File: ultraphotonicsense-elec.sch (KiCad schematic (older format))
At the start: 6 parts, among them J1 Conn_SWD_UART, Q1 BSS138, U1 74HC164

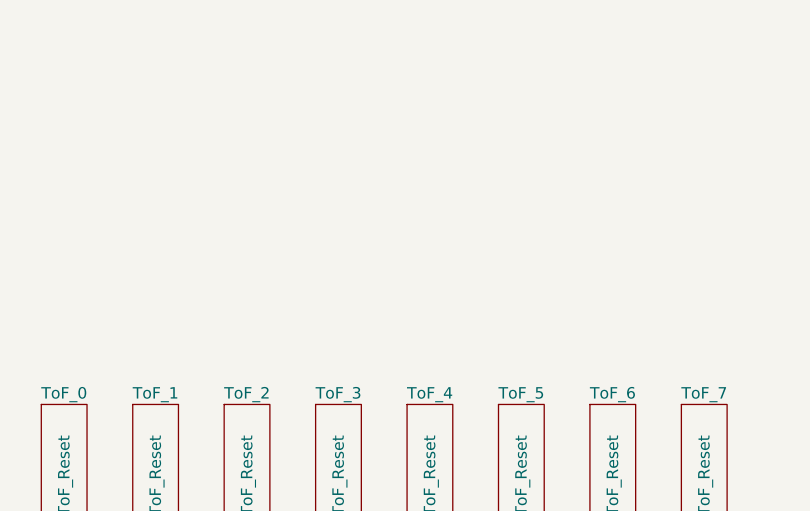
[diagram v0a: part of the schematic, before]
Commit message: Added mounting holes
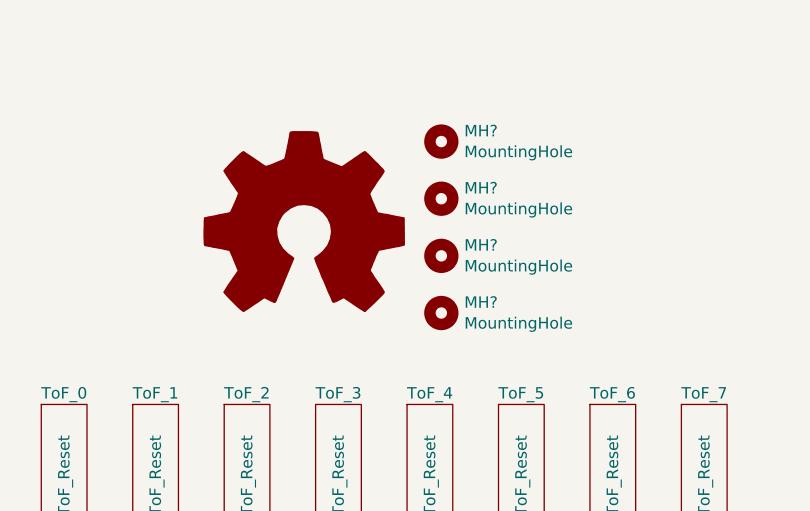
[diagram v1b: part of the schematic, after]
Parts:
- added MH? (x4): MountingHole, symbol Mechanical:MountingHole
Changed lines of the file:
@@
 EESchema Schematic File Version 4
-LIBS:photonicsense-elec-cache
+LIBS:ultraphotonicsense-elec-cache
 EELAYER 26 0
 EELAYER END
@@
 Wire Wire Line
 	1650 3050 1650 2950
+$Comp
+L Graphic:Logo_Open_Hardware_Large #LOGO?
+U 1 1 5BBE6179
+P 8650 3050
+F 0 "#LOGO?" H 8650 3550 50  0001 C CNN
+F 1 "Logo_Open_Hardware_Large" H 8650 2650 50  0001 C CNN
+F 2 "" H 8650 3050 50  0001 C CNN
+F 3 "~" H 8650 3050 50  0001 C CNN
+	1    8650 3050
+	1    0    0    -1
+$EndComp
+$Comp
+L Mechanical:MountingHole MH?
+U 1 1 5BBE6263
+P 9250 2650
+F 0 "MH?" H 9350 2696 50  0000 L CNN
+F 1 "MountingHole" H 9350 2605 50  0000 L CNN
+F 2 "" H 9250 2650 50  0001 C CNN
+F 3 "~" H 9250 2650 50  0001 C CNN
+	1    9250 2650
+	1    0    0    -1
+$EndComp
+$Comp
+L Mechanical:MountingHole MH?
+U 1 1 5BBE62B0
+P 9250 2900
+F 0 "MH?" H 9350 2946 50  0000 L CNN
+F 1 "MountingHole" H 9350 2855 50  0000 L CNN
+F 2 "" H 9250 2900 50  0001 C CNN
+F 3 "~" H 9250 2900 50  0001 C CNN
+	1    9250 2900
+	1    0    0    -1
+$EndComp
+$Comp
+L Mechanical:MountingHole MH?
+U 1 1 5BBE62F0
+P 9250 3150
+F 0 "MH?" H 9350 3196 50  0000 L CNN
+F 1 "MountingHole" H 9350 3105 50  0000 L CNN
+F 2 "" H 9250 3150 50  0001 C CNN
+F 3 "~" H 9250 3150 50  0001 C CNN
+	1    9250 3150
+	1    0    0    -1
+$EndComp
+$Comp
+L Mechanical:MountingHole MH?
+U 1 1 5BBE6333
+P 9250 3400
+F 0 "MH?" H 9350 3446 50  0000 L CNN
+F 1 "MountingHole" H 9350 3355 50  0000 L CNN
+F 2 "" H 9250 3400 50  0001 C CNN
+F 3 "~" H 9250 3400 50  0001 C CNN
+	1    9250 3400
+	1    0    0    -1
+$EndComp
 $EndSCHEMATC

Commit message: Fixed shift register voltage translation
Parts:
- removed Q1: BSS138, Package_TO_SOT_SMD:SOT-23, symbol Transistor_FET:BSS138
- removed R1, R2: R, symbol Device:R
- gave numbers to parts that had none: 4
- renumbered JP2 to JP1
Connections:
- wire segments 70 -> 66

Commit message: Fixed TTa pins issue
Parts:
- removed JP1: Jumper_NC_Dual, symbol Device:Jumper_NC_Dual
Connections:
- net labels removed: US_POWER
- wire segments 66 -> 63

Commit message: Added IC for level translation with ultrasonic sensors
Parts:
- added C1, C2: C, symbol Device:C
- added R1: R, symbol Device:R
- added U1: TXB0108PW, Package_SO:TSSOP-20_4.4x6.5mm_P0.65mm, symbol PhoenixRobotik:TXB0108PW
- J1: footprint (none) -> Connector_JST:JST_XH_S08B-XH-A_1x08_P2.50mm_Horizontal
- MH1, MH2, MH3, MH4: footprint (none) -> MountingHole:MountingHole_2.7mm_M2.5
- U2: renamed from U1; footprint (none) -> Package_SO:SOIC-14_3.9x8.7mm_P1.27mm
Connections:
- wire segments 63 -> 94
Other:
- moved on the sheet: MH1, MH2, MH3, MH4, U2

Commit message: Added ultrasonic sensors power selection
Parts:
- added JP2: Jumper_NC_Dual, symbol Device:Jumper_NC_Dual
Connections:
- net labels added: US_PWR
- wire segments 94 -> 100
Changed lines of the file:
@@
 	5550 2900 5550 3050
-$Comp
-L power:+5V #PWR09
-U 1 1 5BC0FF87
-P 5750 2450
-F 0 "#PWR09" H 5750 2300 50  0001 C CNN
-F 1 "+5V" H 5765 2623 50  0000 C CNN
-F 2 "" H 5750 2450 50  0001 C CNN
-F 3 "" H 5750 2450 50  0001 C CNN
-	1    5750 2450
-	1    0    0    -1
-$EndComp
 $Comp
 L Device:C C1
@@
 	-1   0    0    1
 $EndComp
+Wire Wire Line
+	5350 2900 5550 2900
+Wire Wire Line
+	5550 2900 5550 2450
+Connection ~ 5550 2900
+$Comp
+L power:GND #PWR075
+U 1 1 5BC5DA99
+P 5950 2450
+F 0 "#PWR075" H 5950 2200 50  0001 C CNN
+F 1 "GND" H 5955 2277 50  0000 C CNN
+F 2 "" H 5950 2450 50  0001 C CNN
+F 3 "" H 5950 2450 50  0001 C CNN
+	1    5950 2450
+	-1   0    0    1
+$EndComp
+Wire Wire Line
+	5750 3050 5750 2900
+Wire Wire Line
+	5750 2900 5950 2900
+Connection ~ 5750 2900
+Wire Wire Line
+	5750 2900 5750 2450
+$Comp
+L Device:Jumper_NC_Dual JP2
+U 1 1 5BC62830
+P 1650 2650
+F 0 "JP2" V 1604 2751 50  0000 L CNN
+F 1 "Jumper_NC_Dual" V 1695 2751 50  0000 L CNN
+F 2 "" H 1650 2650 50  0001 C CNN
+F 3 "~" H 1650 2650 50  0001 C CNN
+	1    1650 2650
+	0    1    1    0
+$EndComp
+Text GLabel 1400 2650 0    50   Output ~ 0
+US_PWR
+Wire Wire Line
+	1400 2650 1500 2650
+$Comp
+L power:+5V #PWR09
+U 1 1 5BC6506A
+P 1650 2250
+F 0 "#PWR09" H 1650 2100 50  0001 C CNN
+F 1 "+5V" H 1665 2423 50  0000 C CNN
+F 2 "" H 1650 2250 50  0001 C CNN
+F 3 "" H 1650 2250 50  0001 C CNN
+	1    1650 2250
+	1    0    0    -1
+$EndComp
+Wire Wire Line
+	1650 2250 1650 2400
+$Comp
+L power:+3V3 #PWR048
+U 1 1 5BC678E1
+P 1650 3050
+F 0 "#PWR048" H 1650 2900 50  0001 C CNN
+F 1 "+3V3" H 1665 3223 50  0000 C CNN
+F 2 "" H 1650 3050 50  0001 C CNN
+F 3 "" H 1650 3050 50  0001 C CNN
+	1    1650 3050
+	-1   0    0    1
+$EndComp
+Wire Wire Line
+	1650 2900 1650 3050
 $Comp
 L power:+3.3V #PWR074
@@
 	1    0    0    -1
 $EndComp
-Wire Wire Line
-	5350 2900 5550 2900
-Wire Wire Line
-	5550 2900 5550 2450
-Connection ~ 5550 2900
-$Comp
-L power:GND #PWR075
-U 1 1 5BC5DA99
-P 5950 2450
-F 0 "#PWR075" H 5950 2200 50  0001 C CNN
-F 1 "GND" H 5955 2277 50  0000 C CNN
-F 2 "" H 5950 2450 50  0001 C CNN
-F 3 "" H 5950 2450 50  0001 C CNN
-	1    5950 2450
-	-1   0    0    1
-$EndComp
-Wire Wire Line
-	5750 3050 5750 2900
-Wire Wire Line
-	5750 2900 5950 2900
-Connection ~ 5750 2900
-Wire Wire Line
-	5750 2900 5750 2450
+Text GLabel 5750 2450 1    50   Input ~ 0
+US_PWR
+$Comp
+L power:PWR_FLAG #FLG04
+U 1 1 5BC6A929
+P 1400 2800
+F 0 "#FLG04" H 1400 2875 50  0001 C CNN
+F 1 "PWR_FLAG" V 1400 2928 50  0000 L CNN
+F 2 "" H 1400 2800 50  0001 C CNN
+F 3 "~" H 1400 2800 50  0001 C CNN
+	1    1400 2800
+	0    -1   -1   0
+$EndComp
+Wire Wire Line
+	1500 2650 1500 2800
+Wire Wire Line
+	1500 2800 1400 2800
+Connection ~ 1500 2650
+Wire Wire Line
+	1500 2650 1550 2650
 $EndSCHEMATC

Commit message: Footprint association
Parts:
- C1, C2: footprint (none) -> Capacitor_SMD:C_0805_2012Metric_Pad1.15x1.40mm_HandSolder
- JP2: footprint (none) -> Connector_PinHeader_2.54mm:PinHeader_1x03_P2.54mm_Vertical
- R1: footprint (none) -> Resistor_SMD:R_0805_2012Metric_Pad1.15x1.40mm_HandSolder
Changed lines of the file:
@@
 F 0 "C1" H 5236 2704 50  0000 R CNN
 F 1 "C" H 5236 2795 50  0000 R CNN
-F 2 "" H 5388 2600 50  0001 C CNN
+F 2 "Capacitor_SMD:C_0805_2012Metric_Pad1.15x1.40mm_HandSolder" H 5388 2600 50  0001 C CNN
 F 3 "~" H 5350 2750 50  0001 C CNN
 	1    5350 2750
@@
 F 0 "C2" H 6065 2796 50  0000 L CNN
 F 1 "C" H 6065 2705 50  0000 L CNN
-F 2 "" H 5988 2600 50  0001 C CNN
+F 2 "Capacitor_SMD:C_0805_2012Metric_Pad1.15x1.40mm_HandSolder" H 5988 2600 50  0001 C CNN
 F 3 "~" H 5950 2750 50  0001 C CNN
 	1    5950 2750
@@
 F 0 "R1" H 5120 3146 50  0000 L CNN
 F 1 "R" H 5120 3055 50  0000 L CNN
-F 2 "" V 4980 3100 50  0001 C CNN
+F 2 "Resistor_SMD:R_0805_2012Metric_Pad1.15x1.40mm_HandSolder" V 4980 3100 50  0001 C CNN
 F 3 "~" H 5050 3100 50  0001 C CNN
 	1    5050 3100
@@
 F 0 "JP2" V 1604 2751 50  0000 L CNN
 F 1 "Jumper_NC_Dual" V 1695 2751 50  0000 L CNN
-F 2 "" H 1650 2650 50  0001 C CNN
+F 2 "Connector_PinHeader_2.54mm:PinHeader_1x03_P2.54mm_Vertical" H 1650 2650 50  0001 C CNN
 F 3 "~" H 1650 2650 50  0001 C CNN
 	1    1650 2650

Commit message: Schematic corrections
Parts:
- J1: footprint Connector_JST:JST_XH_S08B-XH-A_1x08_P2.50mm_Horizontal -> Connector_JST:JST_PH_B8B-PH-K_1x08_P2.00mm_Vertical
- renumbered JP2 to JP1
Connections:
- wire segments 100 -> 98
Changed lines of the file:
@@
 $EndSheet
 $Comp
-L power:+3.3V #PWR01
+L power:+3.3V #PWR03
 U 1 1 5BBBF8DE
 P 2300 4050
-F 0 "#PWR01" H 2300 3900 50  0001 C CNN
+F 0 "#PWR03" H 2300 3900 50  0001 C CNN
 F 1 "+3.3V" V 2315 4178 50  0000 L CNN
 F 2 "" H 2300 4050 50  0001 C CNN
@@
 $EndComp
 $Comp
-L power:+2V8 #PWR02
+L power:+2V8 #PWR04
 U 1 1 5BBBF9EE
 P 2300 4150
-F 0 "#PWR02" H 2300 4000 50  0001 C CNN
+F 0 "#PWR04" H 2300 4000 50  0001 C CNN
 F 1 "+2V8" V 2315 4278 50  0000 L CNN
 F 2 "" H 2300 4150 50  0001 C CNN
@@
 F 0 "J1" V 3117 2646 50  0000 C CNN
 F 1 "Conn_SWD_UART" V 3026 2646 50  0000 C CNN
-F 2 "Connector_JST:JST_XH_S08B-XH-A_1x08_P2.50mm_Horizontal" H 2900 2700 50  0001 C CNN
+F 2 "Connector_JST:JST_PH_B8B-PH-K_1x08_P2.00mm_Vertical" H 2900 2700 50  0001 C CNN
 F 3 "~" H 2900 2700 50  0001 C CNN
 	1    2900 2700
@@
 	2900 3700 3550 3700
 $Comp
-L power:GND #PWR05
+L power:GND #PWR07
 U 1 1 5BBC1836
 P 2800 3000
-F 0 "#PWR05" H 2800 2750 50  0001 C CNN
+F 0 "#PWR07" H 2800 2750 50  0001 C CNN
 F 1 "GND" H 2805 2827 50  0000 C CNN
 F 2 "" H 2800 3000 50  0001 C CNN
@@
 	2700 3800 3550 3800
 $Comp
-L power:+3V3 #PWR04
+L power:+3V3 #PWR06
 U 1 1 5BBC19E2
 P 2600 3000
-F 0 "#PWR04" H 2600 2850 50  0001 C CNN
+F 0 "#PWR06" H 2600 2850 50  0001 C CNN
 F 1 "+3V3" H 2615 3173 50  0000 C CNN
 F 2 "" H 2600 3000 50  0001 C CNN
@@
 	1650 4600 1550 4600
 $Comp
-L power:+5V #PWR03
+L power:+5V #PWR05
 U 1 1 5BBF5CE3
 P 2300 4250
-F 0 "#PWR03" H 2300 4100 50  0001 C CNN
+F 0 "#PWR05" H 2300 4100 50  0001 C CNN
 F 1 "+5V" V 2315 4378 50  0000 L CNN
 F 2 "" H 2300 4250 50  0001 C CNN
@@
 	2950 4700 3550 4700
 $Comp
-L power:+2V8 #PWR011
+L power:+2V8 #PWR014
 U 1 1 5BC03D97
 P 7050 4500
-F 0 "#PWR011" H 7050 4350 50  0001 C CNN
+F 0 "#PWR014" H 7050 4350 50  0001 C CNN
 F 1 "+2V8" H 7065 4673 50  0000 C CNN
 F 2 "" H 7050 4500 50  0001 C CNN
@@
 $EndComp
 $Comp
-L power:GND #PWR012
+L power:GND #PWR015
 U 1 1 5BC03E07
 P 7050 6050
-F 0 "#PWR012" H 7050 5800 50  0001 C CNN
+F 0 "#PWR015" H 7050 5800 50  0001 C CNN
 F 1 "GND" H 7055 5877 50  0000 C CNN
 F 2 "" H 7050 6050 50  0001 C CNN
@@
 $EndComp
 $Sheet
-S 6200 2450 300  550
+S 7700 2450 300  550
 U 5BC0526F
 F0 "US_0" 50
 F1 "US.sch" 50
-F2 "Trigger" I B 6300 3000 50
-F3 "Echo" O B 6400 3000 50
-$EndSheet
-$Sheet
-S 6700 2450 300  550
+F2 "Trigger" I B 7900 3000 50
+F3 "Echo" O B 7800 3000 50
+$EndSheet
+$Sheet
+S 7200 2450 300  550
 U 5BC05277
 F0 "US_1" 50
 F1 "US.sch" 50
-F2 "Trigger" I B 6800 3000 50
-F3 "Echo" O B 6900 3000 50
-$EndSheet
-$Sheet
-S 7200 2450 300  550
+F2 "Trigger" I B 7400 3000 50
+F3 "Echo" O B 7300 3000 50
+$EndSheet
+$Sheet
+S 6700 2450 300  550
 U 5BC05284
 F0 "US_2" 50
 F1 "US.sch" 50
-F2 "Trigger" I B 7300 3000 50
-F3 "Echo" O B 7400 3000 50
-$EndSheet
-$Sheet
-S 7700 2450 300  550
+F2 "Trigger" I B 6900 3000 50
+F3 "Echo" O B 6800 3000 50
+$EndSheet
+$Sheet
+S 6200 2450 300  550
 U 5BC05291
 F0 "US_3" 50
 F1 "US.sch" 50
-F2 "Trigger" I B 7800 3000 50
-F3 "Echo" O B 7900 3000 50
+F2 "Trigger" I B 6400 3000 50
+F3 "Echo" O B 6300 3000 50
 $EndSheet
 $Comp
@@
 $EndSheet
 Wire Wire Line
-	6050 5650 6150 5650
-Wire Wire Line
-	6150 5650 6150 5550
-Wire Wire Line
-	6150 5550 6550 5550
-Connection ~ 3450 4300
-Wire Wire Line
 	7050 4500 7050 4650
 $Comp
-L power:+2V8 #PWR010
+L power:+2V8 #PWR013
 U 1 1 5BBFB7FF
 P 6450 5050
-F 0 "#PWR010" H 6450 4900 50  0001 C CNN
+F 0 "#PWR013" H 6450 4900 50  0001 C CNN
 F 1 "+2V8" V 6465 5178 50  0000 L CNN
 F 2 "" H 6450 5050 50  0001 C CNN
@@
 F6 "SWDIO" B L 3550 3700 50
 F7 "SWCLK" I L 3550 3800 50
-F8 "I2C_SCL" B L 3550 4600 50
-F9 "I2C_SDA" B L 3550 4700 50
+F8 "I2C_SCL" B L 3550 4700 50
+F9 "I2C_SDA" B L 3550 4600 50
 F10 "NRST" I L 3550 3600 50
 F11 "TOF_RESET_DATA" O R 4850 4500 50
 F12 "TOF_RESET_SHIFT" O R 4850 4600 50
-F13 "US_TRIG_0" O R 4850 3450 50
-F14 "US_TRIG_1" O R 4850 3650 50
-F15 "US_TRIG_2" O R 4850 3850 50
-F16 "US_TRIG_3" O R 4850 4050 50
-F17 "US_ECHO_0" I R 4850 3550 50
-F18 "US_ECHO_1" I R 4850 3750 50
-F19 "US_ECHO_2" I R 4850 3950 50
-F20 "US_ECHO_3" I R 4850 4150 50
+F13 "US_TRIG_0" O R 4850 4150 50
+F14 "US_TRIG_1" O R 4850 3950 50
+F15 "US_TRIG_2" O R 4850 3750 50
+F16 "US_TRIG_3" O R 4850 3550 50
+F17 "US_ECHO_0" I R 4850 4050 50
+F18 "US_ECHO_1" I R 4850 3850 50
+F19 "US_ECHO_2" I R 4850 3650 50
+F20 "US_ECHO_3" I R 4850 3450 50
 F21 "US_OE" O R 4850 3350 50
 $EndSheet
@@
 	1    0    0    -1
 $EndComp
-Wire Wire Line
-	6150 5300 6150 5250
-Wire Wire Line
-	6150 5250 6550 5250
-Wire Wire Line
-	6050 5300 6150 5300
 $Sheet
 S 5250 5200 800  200
@@
 Wire Wire Line
 	4850 4150 5250 4150
-Wire Wire Line
-	6300 3000 6300 3450
-Wire Wire Line
-	6300 3450 6050 3450
-Wire Wire Line
-	6400 3000 6400 3550
-Wire Wire Line
-	6400 3550 6050 3550
-Wire Wire Line
-	6800 3000 6800 3650
-Wire Wire Line
-	6800 3650 6050 3650
-Wire Wire Line
-	6900 3000 6900 3750
-Wire Wire Line
-	6900 3750 6050 3750
-Wire Wire Line
-	7300 3000 7300 3850
-Wire Wire Line
-	7300 3850 6050 3850
-Wire Wire Line
-	7400 3000 7400 3950
-Wire Wire Line
-	7400 3950 6050 3950
-Wire Wire Line
-	7800 3000 7800 4050
-Wire Wire Line
-	7800 4050 6050 4050
-Wire Wire Line
-	7900 3000 7900 4150
-Wire Wire Line
-	7900 4150 6050 4150
-$Comp
-L power:GND #PWR08
+$Comp
+L power:GND #PWR011
 U 1 1 5BC36ECA
 P 5650 4550
-F 0 "#PWR08" H 5650 4300 50  0001 C CNN
+F 0 "#PWR011" H 5650 4300 50  0001 C CNN
 F 1 "GND" H 5655 4377 50  0000 C CNN
 F 2 "" H 5650 4550 50  0001 C CNN
@@
 	4850 3350 5050 3350
 $Comp
-L power:GND #PWR06
+L power:GND #PWR08
 U 1 1 5BC3D4FD
 P 5050 2850
-F 0 "#PWR06" H 5050 2600 50  0001 C CNN
+F 0 "#PWR08" H 5050 2600 50  0001 C CNN
 F 1 "GND" H 5055 2677 50  0000 C CNN
 F 2 "" H 5050 2850 50  0001 C CNN
@@
 	5050 2850 5050 2950
 Wire Wire Line
-	3450 5650 5250 5650
-Wire Wire Line
-	3450 4300 3450 5650
-Wire Wire Line
 	5250 5300 5000 5300
 Wire Wire Line
@@
 Wire Wire Line
 	5100 4950 5250 4950
-Wire Wire Line
-	5650 4450 5650 4550
-$Comp
-L power:GND #PWR07
+$Comp
+L power:GND #PWR09
 U 1 1 5BC52828
 P 5350 2450
-F 0 "#PWR07" H 5350 2200 50  0001 C CNN
+F 0 "#PWR09" H 5350 2200 50  0001 C CNN
 F 1 "GND" H 5355 2277 50  0000 C CNN
 F 2 "" H 5350 2450 50  0001 C CNN
@@
 Connection ~ 5550 2900
 $Comp
-L power:GND #PWR075
+L power:GND #PWR012
 U 1 1 5BC5DA99
 P 5950 2450
-F 0 "#PWR075" H 5950 2200 50  0001 C CNN
+F 0 "#PWR012" H 5950 2200 50  0001 C CNN
 F 1 "GND" H 5955 2277 50  0000 C CNN
 F 2 "" H 5950 2450 50  0001 C CNN
@@
 	5750 2900 5750 2450
 $Comp
-L Device:Jumper_NC_Dual JP2
+L Device:Jumper_NC_Dual JP1
 U 1 1 5BC62830
 P 1650 2650
-F 0 "JP2" V 1604 2751 50  0000 L CNN
+F 0 "JP1" V 1604 2751 50  0000 L CNN
 F 1 "Jumper_NC_Dual" V 1695 2751 50  0000 L CNN
 F 2 "Connector_PinHeader_2.54mm:PinHeader_1x03_P2.54mm_Vertical" H 1650 2650 50  0001 C CNN
@@
 	1400 2650 1500 2650
 $Comp
-L power:+5V #PWR09
+L power:+5V #PWR01
 U 1 1 5BC6506A
 P 1650 2250
-F 0 "#PWR09" H 1650 2100 50  0001 C CNN
+F 0 "#PWR01" H 1650 2100 50  0001 C CNN
 F 1 "+5V" H 1665 2423 50  0000 C CNN
 F 2 "" H 1650 2250 50  0001 C CNN
@@
 	1650 2250 1650 2400
 $Comp
-L power:+3V3 #PWR048
+L power:+3V3 #PWR02
 U 1 1 5BC678E1
 P 1650 3050
-F 0 "#PWR048" H 1650 2900 50  0001 C CNN
+F 0 "#PWR02" H 1650 2900 50  0001 C CNN
 F 1 "+3V3" H 1665 3223 50  0000 C CNN
 F 2 "" H 1650 3050 50  0001 C CNN
@@
 	1650 2900 1650 3050
 $Comp
-L power:+3.3V #PWR074
+L power:+3.3V #PWR010
 U 1 1 5BC56E1A
 P 5550 2450
-F 0 "#PWR074" H 5550 2300 50  0001 C CNN
+F 0 "#PWR010" H 5550 2300 50  0001 C CNN
 F 1 "+3.3V" H 5565 2623 50  0000 C CNN
 F 2 "" H 5550 2450 50  0001 C CNN
@@
 US_PWR
 $Comp
-L power:PWR_FLAG #FLG04
+L power:PWR_FLAG #FLG01
 U 1 1 5BC6A929
 P 1400 2800
-F 0 "#FLG04" H 1400 2875 50  0001 C CNN
+F 0 "#FLG01" H 1400 2875 50  0001 C CNN
 F 1 "PWR_FLAG" V 1400 2928 50  0000 L CNN
 F 2 "" H 1400 2800 50  0001 C CNN
@@
 Wire Wire Line
 	1500 2650 1550 2650
+Wire Wire Line
+	5650 4450 5650 4550
+Wire Wire Line
+	6400 3550 6050 3550
+Wire Wire Line
+	6400 3000 6400 3550
+Wire Wire Line
+	6300 3450 6050 3450
+Wire Wire Line
+	6300 3000 6300 3450
+Wire Wire Line
+	7900 4150 6050 4150
+Wire Wire Line
+	7900 3000 7900 4150
+Wire Wire Line
+	7800 4050 6050 4050
+Wire Wire Line
+	7800 3000 7800 4050
+Wire Wire Line
+	7400 3950 6050 3950
+Wire Wire Line
+	7400 3000 7400 3950
+Wire Wire Line
+	7300 3850 6050 3850
+Wire Wire Line
+	7300 3000 7300 3850
+Wire Wire Line
+	6900 3750 6050 3750
+Wire Wire Line
+	6900 3000 6900 3750
+Wire Wire Line
+	6800 3650 6050 3650
+Wire Wire Line
+	6800 3000 6800 3650
+Wire Wire Line
+	3450 4300 3450 5650
+Wire Wire Line
+	3450 5650 5250 5650
+Connection ~ 3450 4300
+Wire Wire Line
+	6050 5650 6550 5650
+Wire Wire Line
+	6550 5650 6550 5550
+Wire Wire Line
+	6550 5300 6550 5250
+Wire Wire Line
+	6050 5300 6550 5300
 $EndSCHEMATC

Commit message: PCB routed, no errors but still a few tracks too close
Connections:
- wire segments 98 -> 97
- no-connect marks 1 -> 2
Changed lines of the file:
@@
 Wire Wire Line
 	2700 3800 3550 3800
-$Comp
-L power:+3V3 #PWR06
-U 1 1 5BBC19E2
-P 2600 3000
-F 0 "#PWR06" H 2600 2850 50  0001 C CNN
-F 1 "+3V3" H 2615 3173 50  0000 C CNN
-F 2 "" H 2600 3000 50  0001 C CNN
-F 3 "" H 2600 3000 50  0001 C CNN
-	1    2600 3000
-	-1   0    0    1
-$EndComp
-Wire Wire Line
-	2600 2900 2600 3000
 Wire Wire Line
 	3350 4000 3550 4000
@@
 Wire Wire Line
 	6050 5300 6550 5300
+NoConn ~ 2600 2900
 $EndSCHEMATC
